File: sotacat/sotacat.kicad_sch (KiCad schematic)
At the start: 16 parts, among them J1 54-00035, J2 JST-SH, SW1 SW_SPDT, U1 MOUDLE-SEEEDUINO-XIAO-ESP32C3

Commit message: v0.3 placement
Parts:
- J2: footprint Connector_JST:JST_SH_SM02B-SRSS-TB_1x02-1MP_P1.00mm_Horizontal -> Connector_Molex:Molex_PicoBlade_53261-0271_1x02-1MP_P1.25mm_Horizontal
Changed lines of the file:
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@@
 			)
 		)
-		(property "Footprint" "Connector_JST:JST_SH_SM02B-SRSS-TB_1x02-1MP_P1.00mm_Horizontal"
+		(property "Footprint" "Connector_Molex:Molex_PicoBlade_53261-0271_1x02-1MP_P1.25mm_Horizontal"
 			(at 52.07 55.88 0)
 			(effects

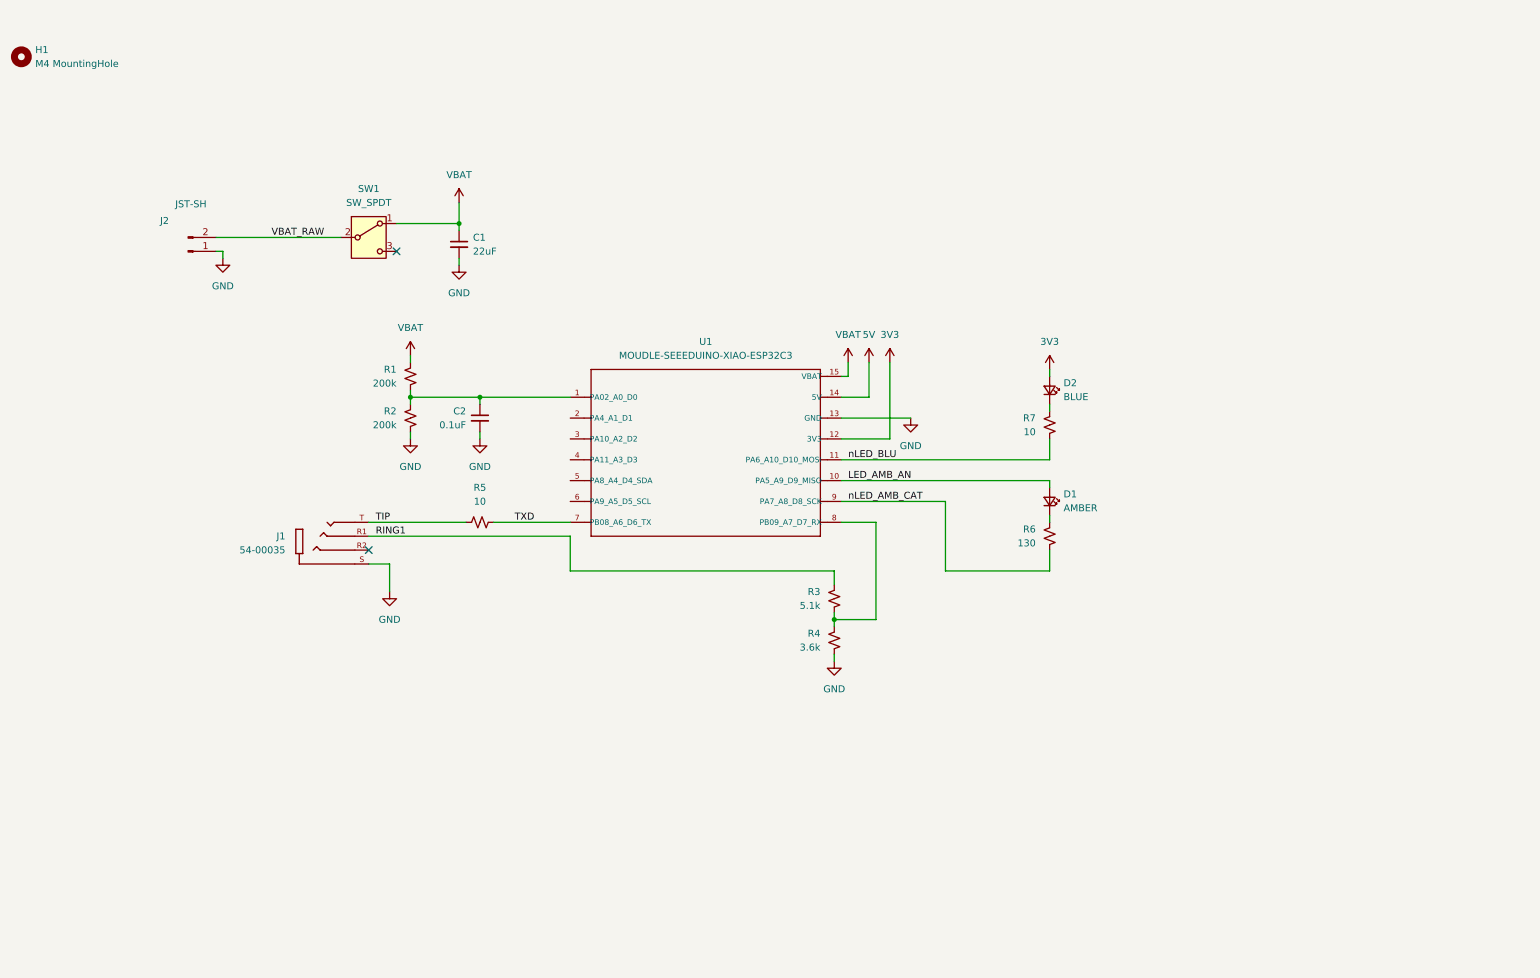
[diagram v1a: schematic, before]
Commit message: Updates for Rev0.3. Breaking pin changes.
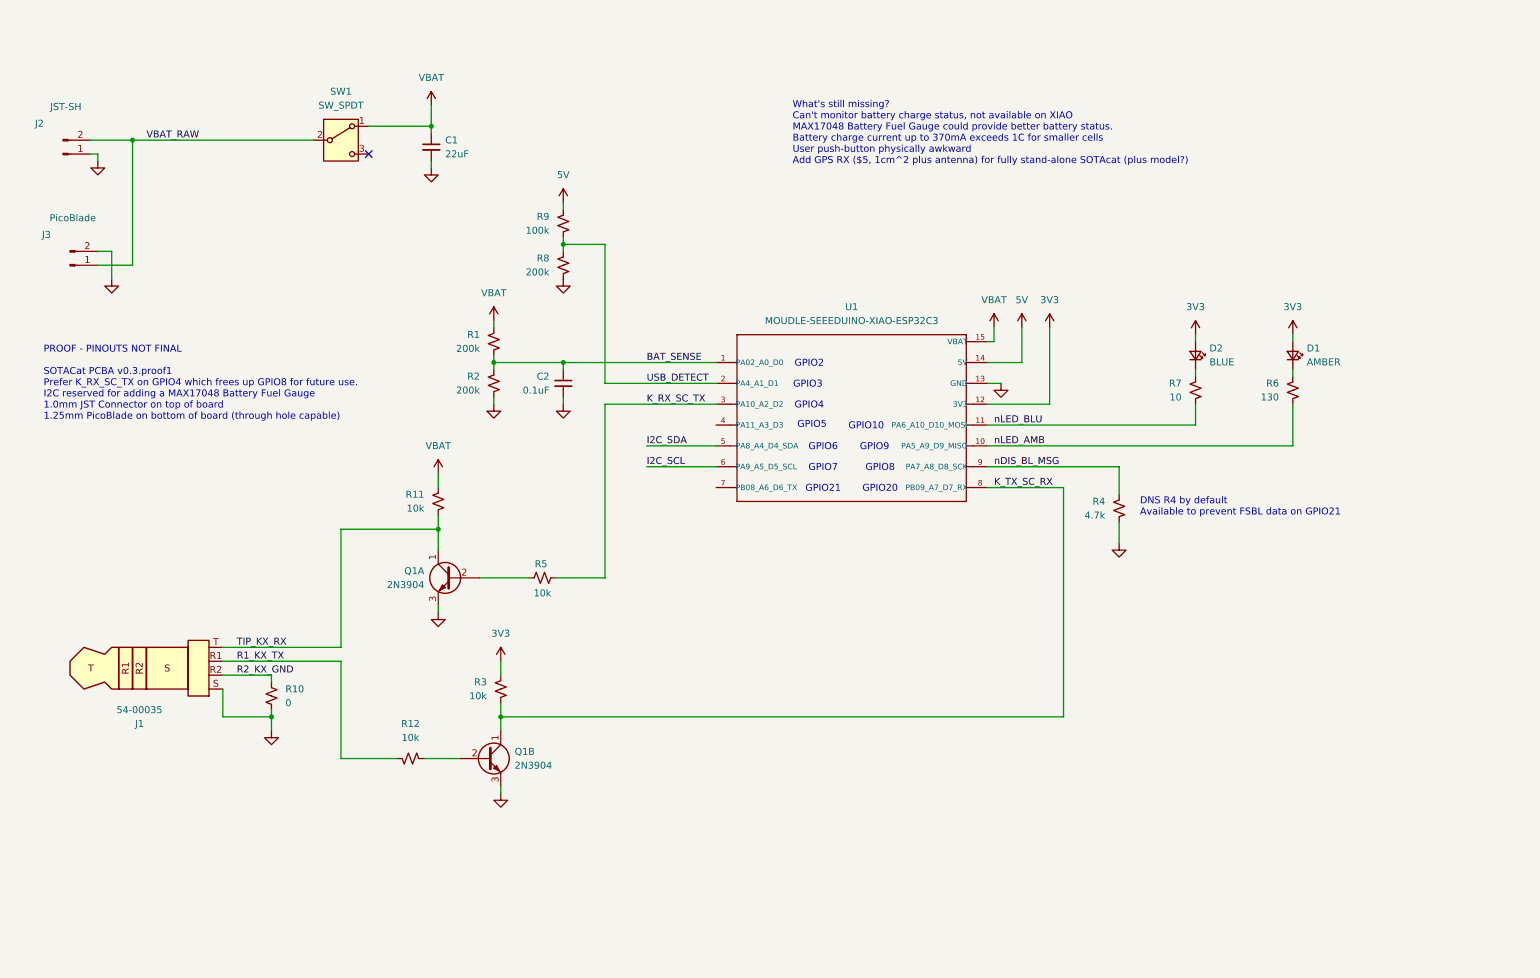
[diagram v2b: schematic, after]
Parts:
- removed H1: M4 MountingHole, MountingHole:MountingHole_4.3mm_M4, symbol Mechanical:MountingHole
- removed J1: 54-00035, TENSITY-AUDIO:TENSILITY_54-00035, symbol TENSITY-AUDIO:54-00035
- added J1: 54-00035, TENSITY-AUDIO:TENSILITY_54-00035, symbol Connector_Audio:AudioPlug4
- added J3: PicoBlade, Connector_Molex:Molex_PicoBlade_53048-0210_1x02_P1.25mm_Horizontal, symbol Connector:Conn_01x02_Pin
- added Q1A, Q1B: 2N3904, symbol Device:Q_NPN_CBE
- added R10: 0, Resistor_SMD:R_0603_1608Metric, symbol Device:R_Small_US
- added R11, R12: 10k, Resistor_SMD:R_0603_1608Metric, symbol Device:R_Small_US
- added R8: 200k, Resistor_SMD:R_0603_1608Metric, symbol Device:R_Small_US
- added R9: 100k, Resistor_SMD:R_0603_1608Metric, symbol Device:R_Small_US
- J2: footprint Connector_Molex:Molex_PicoBlade_53261-0271_1x02-1MP_P1.25mm_Horizontal -> Connector_JST:JST_SH_SM02B-SRSS-TB_1x02-1MP_P1.00mm_Horizontal
- R3: value 5.1k -> 10k
- R4: value 3.6k -> 4.7k; ManPartNo RC0603FR-133K6L -> RT0603DRE07200KL
- R5: value 10 -> 10k
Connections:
- net 3V3: now also D1.2 (A), R3.2
- net 5V: now also R9.1
- net GND: now also J1.S, J3.2 (Pin_2), Q1A.3 (E), Q1B.3 (E), R10.1, R8.2
- net VBAT: now also R11.2
- net VBAT_RAW: now also J3.1 (Pin_1)
- net BAT_SENSE: now reaches C2.1, R1.2, R2.1, U1.1 (PA02_A0_D0)
- net USB_DETECT: now reaches U1.2 (PA4_A1_D1)
- net USB_DETECT: now also R8.1, R9.2
- net K_RX_SC_TX: now reaches U1.3 (PA10_A2_D2)
- net K_RX_SC_TX: now also R5.2
- net I2C_SDA: now reaches U1.5 (PA8_A4_D4_SDA)
- net I2C_SCL: now reaches U1.6 (PA9_A5_D5_SCL)
- net LED_AMB_AN renamed nLED_AMB
- net nLED_AMB: now also R6.2; no longer D1.2 (A)
- net RING1 renamed K_TX_SC_RX
- net K_TX_SC_RX: now also U1.8 (PB09_A7_D7_RX), Q1B.1 (C)
- net TIP: no longer names the net of R5.1
- net TIP: now also Q1A.2 (B)
- net TXD: no longer names the net of U1.7 (PB08_A6_D6_TX)
- net TXD: no longer R5.2
- net nLED_AMB_CAT renamed nDIS_BL_MSG
- net nDIS_BL_MSG: now also R4.1; no longer R6.2
- new net: Q1B.2 (B), R12.1
- new net R1_KX_TX: J1.R1, R12.2
- new net R2_KX_GND: J1.R2, R10.2
- new net TIP_KX_RX: J1.T, Q1A.1 (C), R11.1
- no-connect marks 2 -> 1
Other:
- note added: "DNS R4 by default Available to prevent FSBL data on GPIO21"
- note added: "GPIO10"
- note added: "GPIO2"
- note added: "GPIO20"
- note added: "GPIO21"
- note added: "GPIO3"
- note added: "GPIO4"
- note added: "GPIO5"
- note added: "GPIO6"
- note added: "GPIO7"
- note added: "GPIO8"
- note added: "GPIO9"
- note added: "PROOF - PINOUTS NOT FINAL SOTACat PCBA v0.3.proof1 Prefer K_RX_SC_TX on GPIO4 which frees up GPIO8 for future use. I2C reserved for adding a MAX17048 Battery Fuel Gauge 1.0mm JST Connector on top of board 1.25mm PicoBlade on bottom of board (through hole capable)"
- note added: "What's still missing? Can't monitor battery charge status, not available on XIAO MAX17048 Battery Fuel Gauge could provide better battery status. Battery charge current up to 370mA exceeds 1C for smaller cells User push-button physically awkward Add GPS RX ($5, 1cm^2 plus antenna) for fully stand-alone SOTAcat (plus model?)"
- moved on the sheet: C1, C2, D2, J2, R1, R2, R3, R5, R7, SW1, U1

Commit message: PCB v0.3. Added MAX17260xxTD battery monitor, moved plug to corner, moved switch and LEDs accordingly. Changed pinout. Pinout not compatible with v0.2 due to TX data swap to avoid bootloader output.
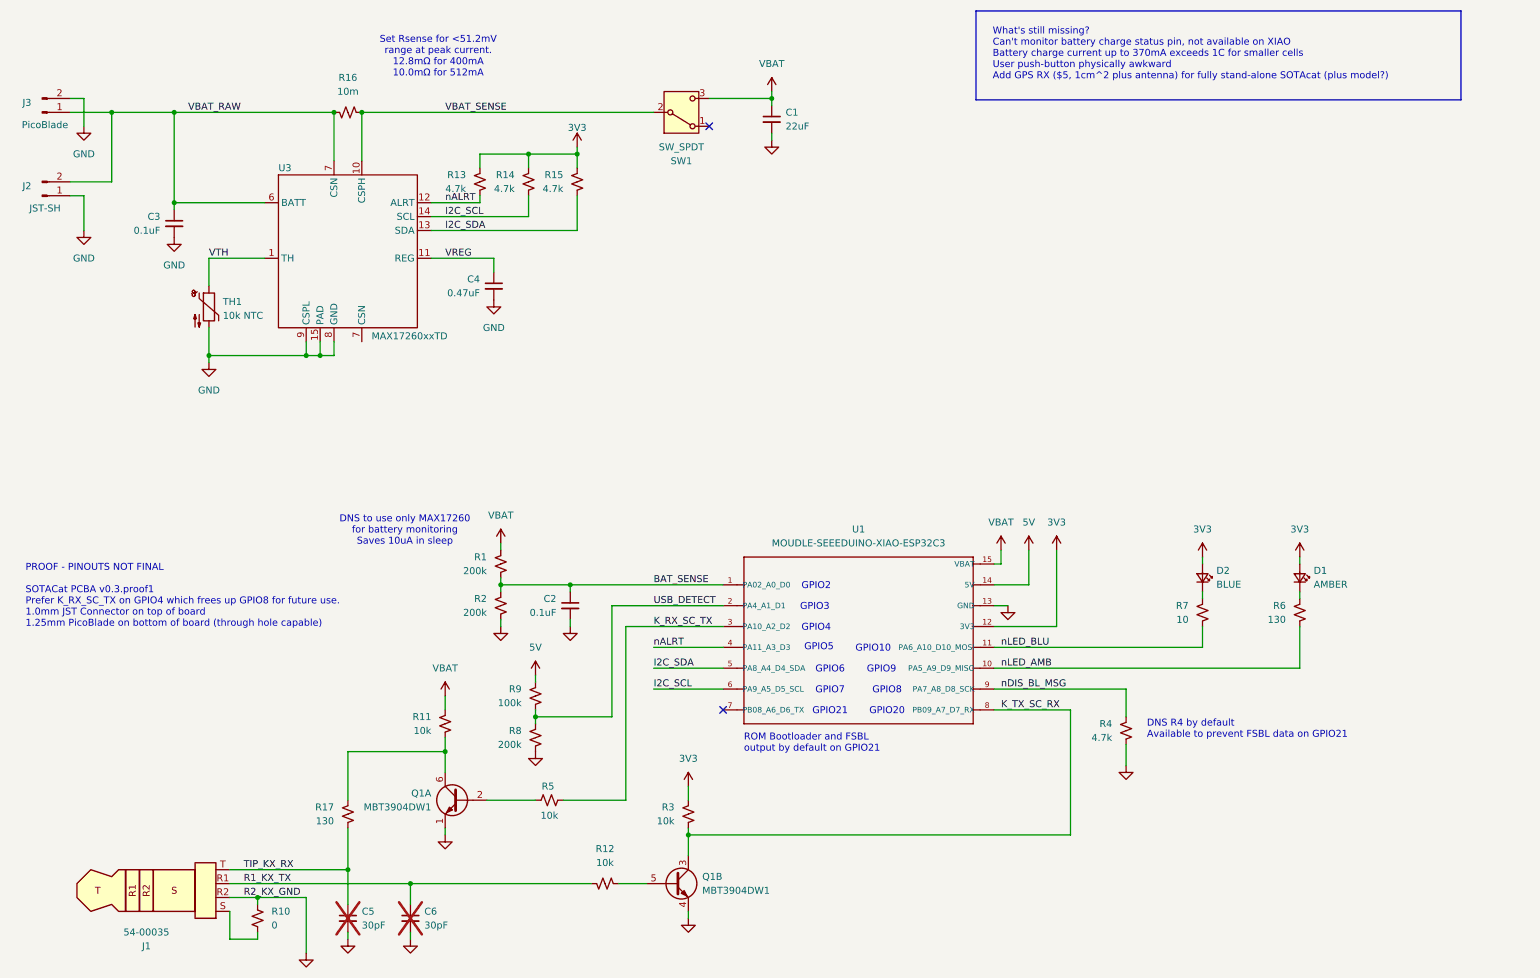
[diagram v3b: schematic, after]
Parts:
- removed Q1A, Q1B: 2N3904, symbol Device:Q_NPN_CBE
- added C3: 0.1uF, Capacitor_SMD:C_0603_1608Metric, symbol Device:C_Small
- added C4: 0.47uF, Capacitor_SMD:C_0603_1608Metric, symbol Device:C_Small
- added C5, C6: 30pF, Capacitor_SMD:C_0402_1005Metric, symbol Device:C_Small
- added Q1: MBT3904DW1, Package_TO_SOT_SMD:SOT-363_SC-70-6, symbol Transistor_BJT:MBT3904DW1
- added R13, R14, R15: 4.7k, Resistor_SMD:R_0603_1608Metric, symbol Device:R_Small_US
- added R16: 10m, Resistor_SMD:R_0603_1608Metric, symbol Device:R_Small_US
- added R17: 130, Resistor_SMD:R_0603_1608Metric, symbol Device:R_Small_US
- added TH1: 10k NTC, Resistor_SMD:R_0603_1608Metric, symbol Device:Thermistor_NTC
- added U3: MAX17260xxTD, Package_DFN_QFN:TDFN-14-1EP_3x3mm_P0.4mm_EP1.78x2.35mm, symbol sotacat-lib:MAX17260SETD
- C1: JLPCBPN (none) -> C92819; ManPartNo2 (none) -> LMK316BJ226ML-T; Manufacturer2 (none) -> Taiyo Yuden
- C2: JLPCBPN (none) -> C14663; ManPartNo2 (none) -> CC0603KRX7R9BB104; Manufacturer2 (none) -> YAGEO
- D1: JLPCBPN (none) -> C2690338; ManPartNo2 (none) -> SML-D12D1WT86; Manufacturer2 (none) -> ROHM Semicon
- D2: JLPCBPN (none) -> C72041; ManPartNo2 (none) -> 19-217/BHC-ZL1M2RY/3T; Manufacturer2 (none) -> Everlight Elec
- J2: footprint Connector_JST:JST_SH_SM02B-SRSS-TB_1x02-1MP_P1.00mm_Horizontal -> Connector_JST:JST_SH_SM02B-SRSS-TB_1x02-1MP_P1.00mm_Horizontal; ManPartNo ‎SM02B-SRSS-TB‎ -> SM02B-SRSS-TB; Manufacturer JST -> JST-SH
- R10: JLPCBPN (none) -> C21189; ManPartNo2 (none) -> 0603WAF0000T5E; Manufacturer2 (none) -> UNI-ROYAL(Uniroyal Elec)
- R11, R12, R3: JLPCBPN (none) -> C25804; ManPartNo RC0603FR-135K1L -> RT0603FRE0710KL; ManPartNo2 (none) -> 0603WAF1002T5E; Manufacturer2 (none) -> UNI-ROYAL(Uniroyal Elec)
- R4: JLPCBPN (none) -> C23162; ManPartNo2 (none) -> 0603WAF4701T5E; Manufacturer2 (none) -> UNI-ROYAL(Uniroyal Elec)
- R5: JLPCBPN (none) -> C25804; ManPartNo RC0603FR-0710RL -> RT0603FRE0710KL; ManPartNo2 (none) -> 0603WAF1002T5E; Manufacturer2 (none) -> UNI-ROYAL(Uniroyal Elec)
- R6: JLPCBPN (none) -> C22798; ManPartNo2 (none) -> 0603WAF130JT5E; Manufacturer2 (none) -> UNI-ROYAL(Uniroyal Elec)
- R7: JLPCBPN (none) -> C138286; ManPartNo2 (none) -> AC0603FR-0710RL; Manufacturer2 (none) -> YAGEO
- R9: JLPCBPN (none) -> C25803; ManPartNo2 (none) -> 0603WAF1003T5E; Manufacturer2 (none) -> UNI-ROYAL(Uniroyal Elec)
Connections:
- net R2_KX_GND is gone; now on net GND: J1.R2, R10.2
- net 3V3: now also R13.1, R14.1, R15.1
- net GND: now also C3.2, C4.2, C5.2, C6.2, Q1.1 (E1), Q1.4 (E2), TH1.2, U3.15 (PAD), U3.8 (GND), U3.9 (CSPL); no longer J1.S, R10.1
- net I2C_SCL: now also R14.2, U3.14 (SCL)
- net I2C_SDA: now also R15.2, U3.13 (SDA)
- net K_TX_SC_RX: now also Q1.3 (C2)
- net R1_KX_TX: now also C6.1
- net TIP_KX_RX: now also C5.1, R17.2; no longer R11.1
- net VBAT: now also SW1.3 (C); no longer SW1.1 (A)
- net VBAT_RAW: now also C3.1, R16.1, U3.6 (BATT), U3.7 (CSN); no longer SW1.2 (B)
- net at R5.1: now also Q1.2 (B1)
- net nALRT: now reaches U1.4 (PA11_A3_D3)
- net nALRT: now also R13.2, U3.12 (ALRT)
- net at R12.1: now also Q1.5 (B2)
- new net: J1.S, R10.1
- new net: Q1.6 (C1), R11.1, R17.1
- new net VBAT_SENSE: R16.2, SW1.2 (B), U3.10 (CSPH)
- new net VREG: C4.1, U3.11 (REG)
- new net VTH: TH1.1, U3.1 (TH)
- no-connect marks 1 -> 2
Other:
- note added: "DNS to use only MAX17260 for battery monitoring Saves 10uA in sleep"
- note added: "PROOF - PINOUTS NOT FINAL SOTACat PCBA v0.3.proof1 Prefer K_RX_SC_TX on GPIO4 which frees up GPIO8 for future use. 1.0mm JST Connector on top of board 1.25mm PicoBlade on bottom of board (through hole capable)"
- note added: "ROM Bootloader and FSBL output by default on GPIO21"
- note added: "Set Rsense for <51.2mV range at peak current. 12.8mΩ for 400mA 10.0mΩ for 512mA"
- note added: "What's still missing? Can't monitor battery charge status pin, not available on XIAO Battery charge current up to 370mA exceeds 1C for smaller cells User push-button physically awkward Add GPS RX ($5, 1cm^2 plus antenna) for fully stand-alone SOTAcat (plus model?)"
- note removed: "PROOF - PINOUTS NOT FINAL SOTACat PCBA v0.3.proof1 Prefer K_RX_SC_TX on GPIO4 which frees up GPIO8 for future use. I2C reserved for adding a MAX17048 Battery Fuel Gauge 1.0mm JST Connector on top of board 1.25mm PicoBlade on bottom of board (through hole capable)"
- note removed: "What's still missing? Can't monitor battery charge status, not available on XIAO MAX17048 Battery Fuel Gauge could provide better battery status. Battery charge current up to 370mA exceeds 1C for smaller cells User push-button physically awkward Add GPS RX ($5, 1cm^2 plus antenna) for fully stand-alone SOTAcat (plus model?)"
- moved on the sheet: C2, D1, D2, J1, J3, R1, R10, R11, R2, R3, R4, R5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
